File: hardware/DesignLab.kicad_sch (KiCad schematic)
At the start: 79 parts

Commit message: Update BOM
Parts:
- BT1, BT2, BT3, BT4: Stock en EC (none) -> No; manf# (none) -> 534-2477; provedor (none) -> MOUSER
- RV1: LCSC# C99198 -> (none); Stock en EC Yes -> No; manf# (none) -> MCP4017T-103E/LT; provedor LCSC -> MOUSER
- SW1, SW13, SW2: Stock en EC (none) -> No; manf# (none) -> JS102011SAQN; provedor (none) -> MOUSER
- SW10, SW11, SW3, SW4, SW5, SW6, SW7, SW8, SW9: Stock en EC (none) -> No; manf# (none) -> EVQ-PLFA08; provedor (none) -> MOUSER
- SW12: Stock en EC (none) -> No; manf# (none) -> TL3342F450QG; provedor (none) -> MOUSER
- U2: provedor (none) -> MOUSER
- U3, U4, U5: manf# QRE1113GR -> QRE1113; provedor LCSC -> MOUSER
- U6: manf# AT25SF128A-MHB-T -> AT25SF128A-SHB-T
- U8: LCSC# C51118 -> (none); manf# AP2112K-3.3TRG1 -> AP7347DQ-33W5-7; provedor LCSC -> MOUSER

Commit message: Add Micro SD, digital Pot
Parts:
- removed BT1, BT2, BT3: (no value), symbol Device:Battery_Cell
- removed RV1: (no value), symbol Device:R_Potentiometer
- added C?: 100nF, Capacitor_SMD:C_0603_1608Metric, symbol Device:C_Small
- added J?: Micro_SD_Card_Det, symbol Connector:Micro_SD_Card_Det
- added R?: 100K, symbol Device:R_Small
- added SW?: Button, symbol Switch:SW_Push
- added U?: MCP4018-xxxxLT, Package_TO_SOT_SMD:SOT-363_SC-70-6, symbol Potentiometer_Digital:MCP4018-xxxxLT
- BT4: value (none) -> Battery_Cell
- BZ1: value (none) -> Buzzer
- C1, C3: value (none) -> 27pF; footprint (none) -> Capacitor_SMD:C_0603_1608Metric
- C10, C11, C12, C13, C14, C15, C16, C5, C6, C8, C9: value (none) -> 100nF; footprint (none) -> Capacitor_SMD:C_0402_1005Metric_Pad0.74x0.62mm_HandSolder
- C17, C18, C19: value (none) -> 10nF; footprint (none) -> Capacitor_SMD:C_0603_1608Metric
- C2: value (none) -> 0.1uF; footprint (none) -> Capacitor_SMD:C_0402_1005Metric_Pad0.74x0.62mm_HandSolder
- C20: value (none) -> 47uF; footprint (none) -> Capacitor_SMD:C_0603_1608Metric
- C21, C22, C4, C7: value (none) -> 1uF; footprint (none) -> Capacitor_SMD:C_0603_1608Metric
- C23, C24: value (none) -> 220pF; footprint (none) -> Capacitor_SMD:C_0603_1608Metric
- C25, C26, C27: value (none) -> 10uF; footprint (none) -> Capacitor_SMD:C_0402_1005Metric_Pad0.74x0.62mm_HandSolder
- D1: value (none) -> MBR120; footprint (none) -> Diode_SMD:D_SOD-123F
- F1: value (none) -> 0.5A; footprint (none) -> Fuse:Fuse_0805_2012Metric
- JP1: value (none) -> BOOT; footprint (none) -> Jumper:SolderJumper-2_P1.3mm_Open_Pad1.0x1.5mm
- P1: value (none) -> USB_C_Plug_USB2.0; footprint (none) -> Connectors:C393939
- Q1: value (none) -> DMG3415U-7; footprint (none) -> Package_TO_SOT_SMD:SOT-23
- R1: value (none) -> 1K; footprint (none) -> Resistor_SMD:R_0603_1608Metric
- R10, R11, R12: value (none) -> 220; footprint (none) -> Capacitor_SMD:C_0603_1608Metric
- R13: value (none) -> 1.8K; footprint (none) -> Resistor_SMD:R_0603_1608Metric
- R14, R15, R9: value (none) -> 100; footprint (none) -> Resistor_SMD:R_0603_1608Metric
- R16: value (none) -> 10K; footprint (none) -> Resistor_SMD:R_0603_1608Metric
- R17: value (none) -> 100K; footprint (none) -> Resistor_SMD:R_0603_1608Metric
- R18, R19: value (none) -> 5k1; footprint (none) -> Resistor_SMD:R_0603_1608Metric
- R2, R3: value (none) -> 27; footprint (none) -> Resistor_SMD:R_0603_1608Metric
- R4, R6, R7: value (none) -> 100; footprint (none) -> Capacitor_SMD:C_0603_1608Metric
- R5: value (none) -> 4K7; footprint (none) -> Resistor_SMD:R_0603_1608Metric
- R8: value (none) -> 220; footprint (none) -> Resistor_SMD:R_0603_1608Metric
- SW1, SW2: value (none) -> SW_DPDT_x2
- SW10, SW11, SW3, SW4, SW5, SW6, SW7, SW8, SW9: value (none) -> Button
- SW12: value (none) -> RESET
- SW13: value (none) -> ON
- U1: value (none) -> SPH0641LM4H; footprint (none) -> Sensors:MIC_SPH0641LM4H-1
- U2: value (none) -> RP2040; footprint (none) -> badge_pwnCon:RP2040-QFN-56
- U3, U4, U5: value (none) -> QRE1113; footprint (none) -> Package_DIP:SMDIP-4_W7.62mm
- U6: value (none) -> AT25SF128A
- U7: value (none) -> PAM8302AAD; footprint (none) -> Package_SO:MSOP-8_3x3mm_P0.65mm
- U8: value (none) -> AP2112K-3.3; footprint (none) -> Package_TO_SOT_SMD:SOT-23-5
- Y1: value (none) -> 12Mhz; footprint (none) -> Crystal:Crystal_SMD_HC49-SD
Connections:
- net +3V3: now also C?.1, J?.4 (VDD), R?.1, U?.1 (VDD)
- net D4: now also U2.4 (GPIO2); no longer U2.28 (GPIO17)
- net GND: now also BT4.2 (-), C?.2, J?.11 (SHIELD), J?.6 (VSS), J?.9 (DET_B), SW?.1, U?.2 (VSS)
- net GP18: now also U2.17 (GPIO14); no longer U2.29 (GPIO18)
- net REC: now also U2.5 (GPIO3); no longer U2.7 (GPIO5)
- net A: now reaches C20.2, R13.1
- net A: now also U?.6 (A)
- net at C21.1: now also U?.5 (W)
- net CD: now reaches U2.18 (GPIO15)
- net CD: now also J?.10 (DET_A)
- net CIPO: now reaches U2.27 (GPIO16)
- net CIPO: now also J?.7 (DAT0)
- net VOL: now reaches U2.3 (GPIO1)
- net VOL: now also SW?.2
- net COPI: now reaches U2.30 (GPIO19)
- net COPI: now also J?.3 (CMD)
- net SDA: now reaches U2.6 (GPIO4)
- net SDA: now also U?.3 (SCL)
- new net CS: J?.2 (DAT3/CD), R?.2, U2.28 (GPIO17)
- new net CSK: J?.5 (CLK)
- new net SCK: U2.29 (GPIO18)
- new net SCL: U2.7 (GPIO5), U?.4 (SDA)
- no-connect marks 12 -> 9
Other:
- note removed: "Cambiar por AT25SF128A-MHB-T con emapque compatible"
- moved on the sheet: BZ1, C15, C16, C17, C18, C19, C20, C21, C22, C23, C24, C25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

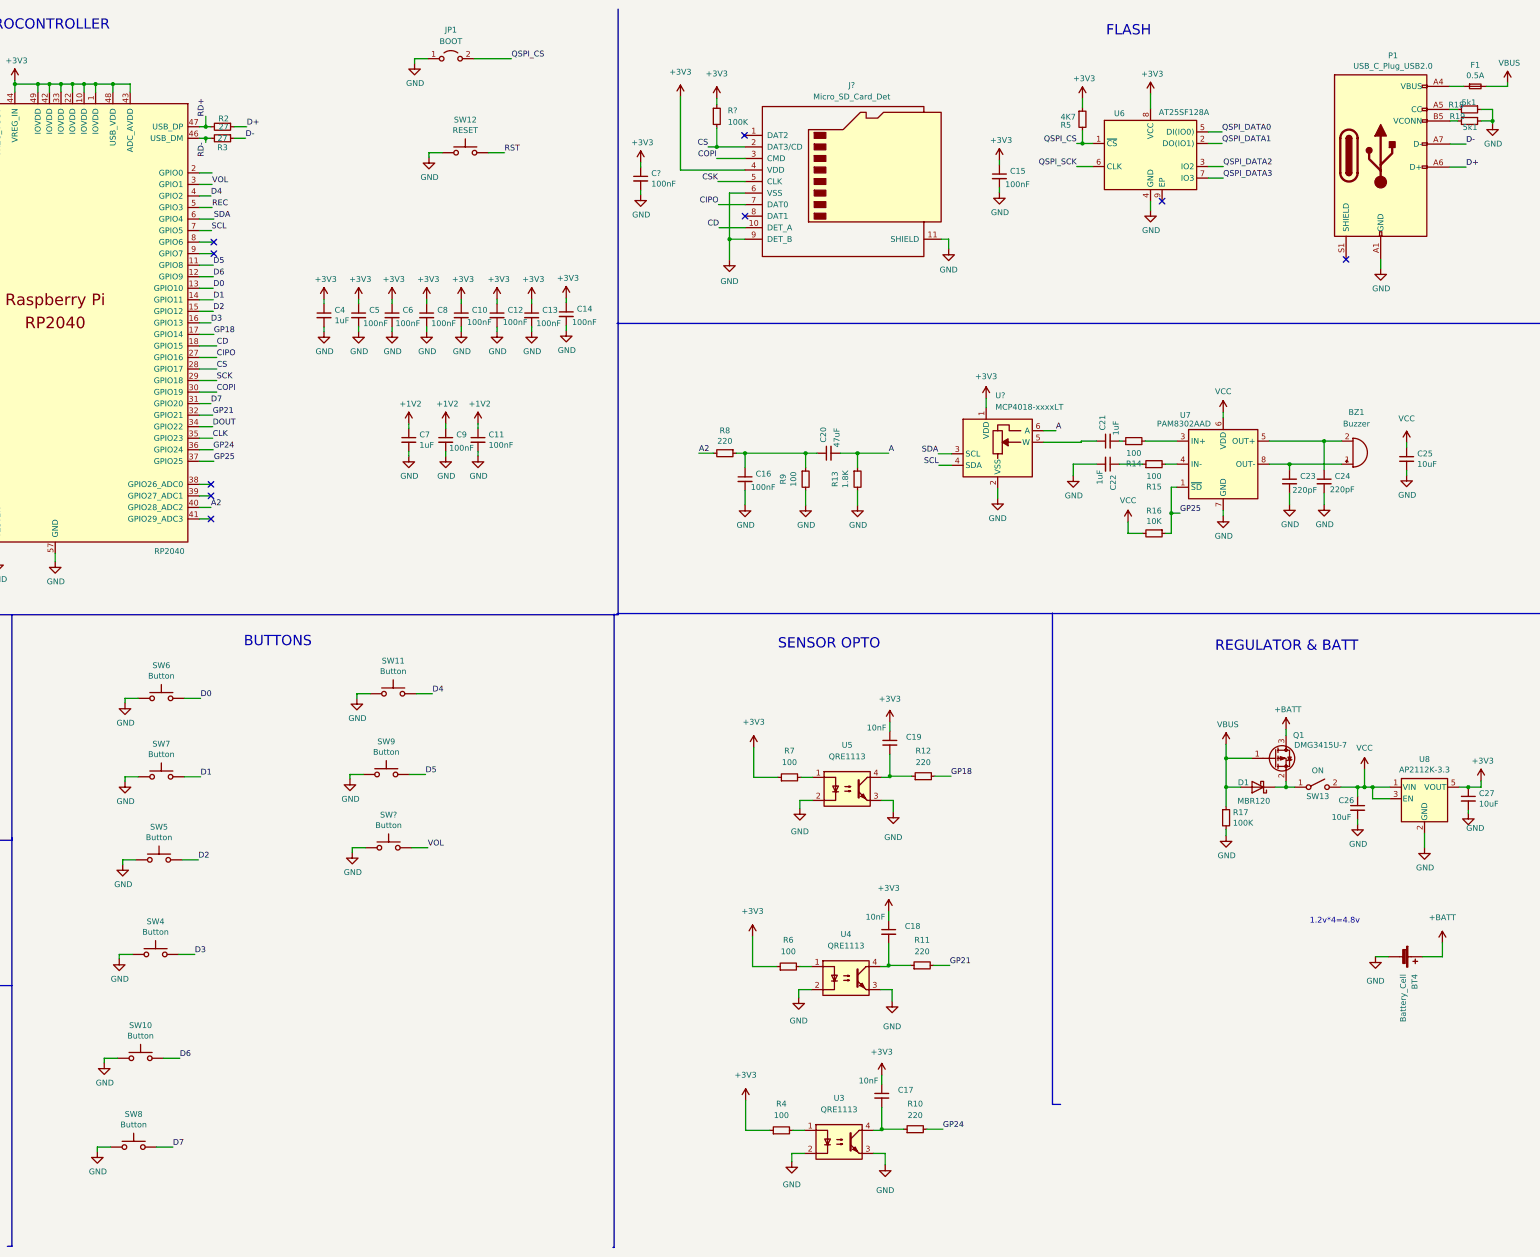
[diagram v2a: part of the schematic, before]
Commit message: add sensor and change button reset
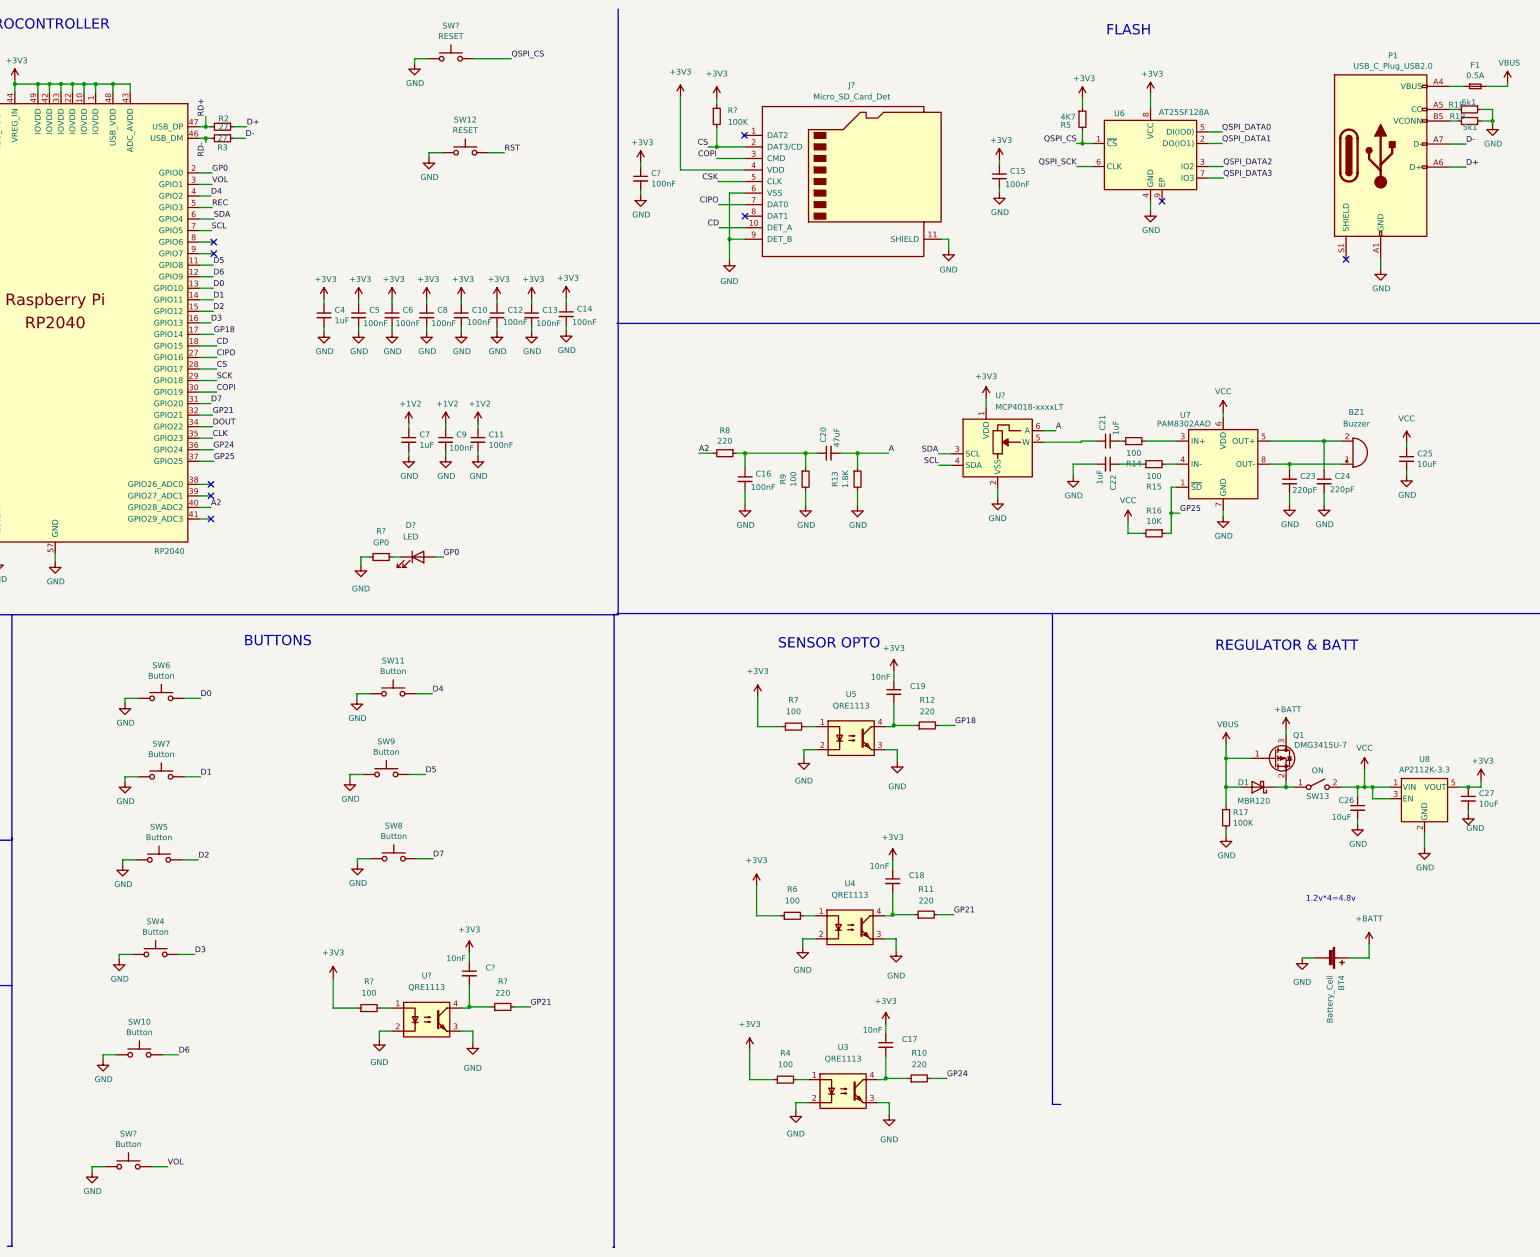
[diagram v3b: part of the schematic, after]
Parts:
- removed JP1: BOOT, Jumper:SolderJumper-2_P1.3mm_Open_Pad1.0x1.5mm, symbol Jumper:Jumper_2_Open
- added C?: 10nF, Capacitor_SMD:C_0603_1608Metric, symbol Device:C_Small
- added D?: LED, symbol Device:LED
- added R?: GP0, symbol Device:R_Small
- added R?: 220, Capacitor_SMD:C_0603_1608Metric, symbol Device:R_Small
- added R?: 100, Capacitor_SMD:C_0603_1608Metric, symbol Device:R_Small
- added SW?: RESET, symbol Switch:SW_Push
- added U?: QRE1113, Package_DIP:SMDIP-4_W7.62mm, symbol Isolator:SFH617A-2X009T
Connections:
- net +3V3: now also C?.1, R?.1
- net GND: now also R?.2, SW?.1, U?.2, U?.3
- net GP21: now also R?.2
- net QSPI_CS: now also SW?.2
- net GP0: now reaches U2.2 (GPIO0)
- net GP0: now also D?.2 (A)
- new net: D?.1 (K), R?.1
- new net: C?.2, R?.1, U?.4
- new net: R?.2, U?.1
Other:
- moved on the sheet: BT4, C17, C18, C19, R10, R11, R12, R4, R6, R7, SW10, SW8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

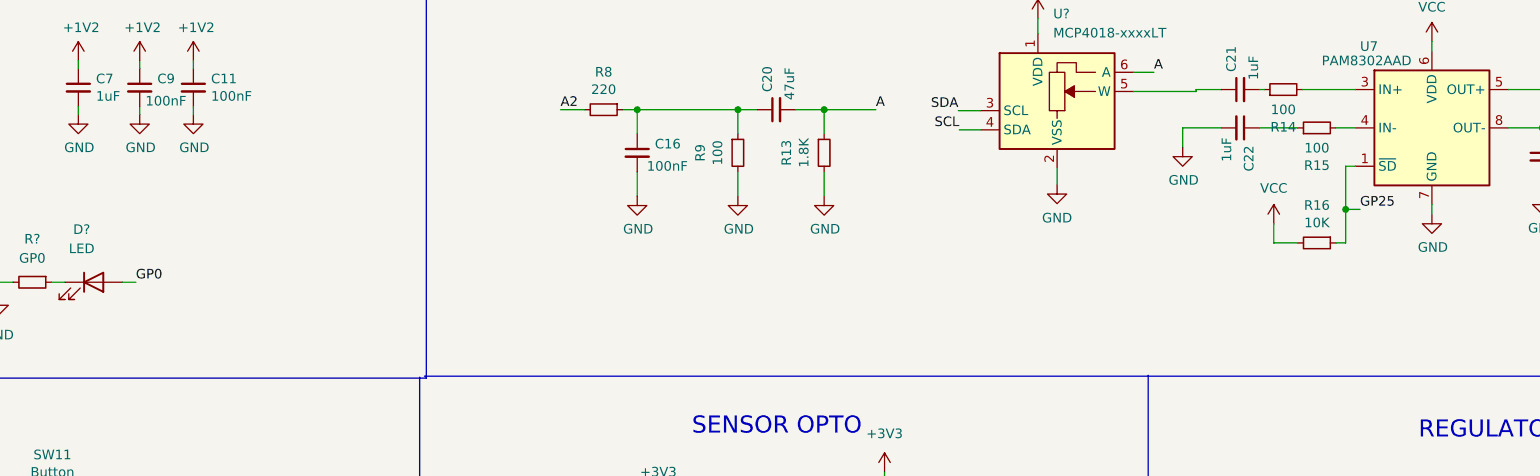
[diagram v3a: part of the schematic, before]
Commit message: change LED_BUILTIN
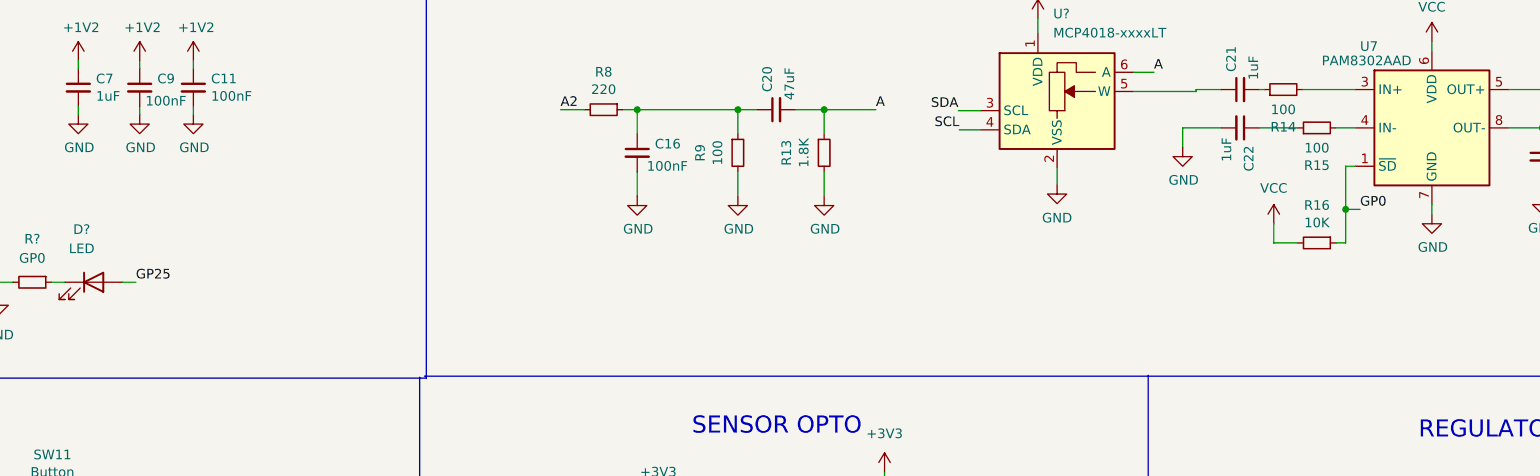
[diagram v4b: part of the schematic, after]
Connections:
- net GP0: now also R16.1, U7.1 (~{SD}); no longer D?.2 (A)
- net GP25: now also D?.2 (A); no longer R16.1, U7.1 (~{SD})
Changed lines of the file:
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@@
     (effects (font (size 1.27 1.27)) (justify left bottom))
   )
-  (label "GP25" (at 327.279 123.063 0)
+  (label "GP0" (at 327.279 123.063 0)
     (effects (font (size 1.27 1.27)) (justify left bottom))
   )
@@
     (effects (font (size 1.27 1.27)) (justify left bottom))
   )
-  (label "GP0" (at 165.1 132.715 0)
+  (label "GP25" (at 165.1 132.715 0)
     (effects (font (size 1.27 1.27)) (justify left bottom))
   )

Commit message: fix buttons
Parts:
- added J?: Conn_01x04_Female, symbol Connector:Conn_01x04_Female
- R?: value GP0 -> 330
- SW?: value RESET -> BOOT
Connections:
- net GP18 is gone; now on net S1: R12.2, U2.17 (GPIO14)
- net +3V3: now also J?.1 (Pin_1)
- net GND: now also J?.4 (Pin_4)
- net SWCLK: now also J?.2 (Pin_2)
- net SWDIO: now also J?.3 (Pin_3)
- net LANG: now reaches U2.38 (GPIO26_ADC0)
- net LANG: now also SW2.2 (B)
- net WORD: now reaches U2.39 (GPIO27_ADC1)
- net WORD: now also SW1.2 (B)
- net S4: now reaches U2.8 (GPIO6)
- net S4: now also R?.2
- removed net GP: SW1.2 (B), SW2.2 (B)
- net GP0 renamed S1
- net S1: no longer U2.2 (GPIO0)
- removed net GP21: R11.2, R?.2, U2.32 (GPIO21)
- net GP24 renamed S2
- net S2: now also R11.2; no longer R10.2
- new net EN_SOUND: U2.2 (GPIO0)
- new net S3: R10.2, U2.32 (GPIO21)
- no-connect marks 9 -> 6
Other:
- note added: "SWD"
- moved on the sheet: BT4, C26, C27, C?, D1, Q1, R17, R?, SW13, U8, U?

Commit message: Assigned footprints
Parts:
- BT4: value Battery_Cell -> (none)
- BZ1: value Buzzer -> (none)
- C1, C3: value 27pF -> (none); footprint Capacitor_SMD:C_0603_1608Metric -> (none)
- C10, C11, C12, C13, C14, C15, C16, C5, C6, C8, C9: value 100nF -> (none); footprint Capacitor_SMD:C_0402_1005Metric_Pad0.74x0.62mm_HandSolder -> (none)
- C17, C18, C19: value 10nF -> (none); footprint Capacitor_SMD:C_0603_1608Metric -> (none)
- C2: value 0.1uF -> (none); footprint Capacitor_SMD:C_0402_1005Metric_Pad0.74x0.62mm_HandSolder -> (none)
- C20: value 47uF -> (none); footprint Capacitor_SMD:C_0603_1608Metric -> (none)
- C21, C22, C4, C7: value 1uF -> (none); footprint Capacitor_SMD:C_0603_1608Metric -> (none)
- C23, C24: value 220pF -> (none); footprint Capacitor_SMD:C_0603_1608Metric -> (none)
- C25, C26, C27: value 10uF -> (none); footprint Capacitor_SMD:C_0402_1005Metric_Pad0.74x0.62mm_HandSolder -> (none)
- C28: renamed from C?; value 10nF -> (none); footprint Capacitor_SMD:C_0603_1608Metric -> (none)
- C29: renamed from C?; value 100nF -> (none); footprint Capacitor_SMD:C_0603_1608Metric -> (none); LCSC# C26413 -> C106209; manf# CL10A105KP8NNNC -> CC0402ZRY5V7BB104
- D1: value MBR120 -> (none); footprint Diode_SMD:D_SOD-123F -> (none)
- D2: renamed from D?; value LED -> (none)
- F1: value 0.5A -> (none); footprint Fuse:Fuse_0805_2012Metric -> (none)
- J1: renamed from J?; value Micro_SD_Card_Det -> (none); Stock en EC (none) -> No
- J2: renamed from J?; value Conn_01x04_Female -> (none)
- P1: value USB_C_Plug_USB2.0 -> (none); footprint Connectors:C393939 -> (none)
- Q1: value DMG3415U-7 -> (none); footprint Package_TO_SOT_SMD:SOT-23 -> (none)
- R1: value 1K -> (none); footprint Resistor_SMD:R_0603_1608Metric -> (none)
- R10, R11, R12: value 220 -> (none); footprint Capacitor_SMD:C_0603_1608Metric -> (none)
- R13: value 1.8K -> (none); footprint Resistor_SMD:R_0603_1608Metric -> (none)
- R14, R15, R9: value 100 -> (none); footprint Resistor_SMD:R_0603_1608Metric -> (none)
- R16: value 10K -> (none); footprint Resistor_SMD:R_0603_1608Metric -> (none)
- R17: value 100K -> (none); footprint Resistor_SMD:R_0603_1608Metric -> (none); manf# RC0603JR-07100KL -> (none)
- R18, R19: value 5k1 -> (none); footprint Resistor_SMD:R_0603_1608Metric -> (none)
- R2, R3: value 27 -> (none); footprint Resistor_SMD:R_0603_1608Metric -> (none)
- R20: renamed from R?; value 330 -> (none)
- R21: renamed from R?; value 100 -> (none); footprint Capacitor_SMD:C_0603_1608Metric -> (none)
- R22: renamed from R?; value 220 -> (none); footprint Capacitor_SMD:C_0603_1608Metric -> (none)
- R23: renamed from R?; value 100K -> (none); LCSC# (none) -> C100048; Stock en EC (none) -> Yes; provedor (none) -> LCSC
- R4, R6, R7: value 100 -> (none); footprint Capacitor_SMD:C_0603_1608Metric -> (none)
- R5: value 4K7 -> (none); footprint Resistor_SMD:R_0603_1608Metric -> (none)
- R8: value 220 -> (none); footprint Resistor_SMD:R_0603_1608Metric -> (none)
- SW1, SW2: value SW_DPDT_x2 -> (none); manf# JS102011SAQN -> (none)
- SW10, SW11, SW3, SW4, SW5, SW6, SW7, SW8, SW9: value Button -> (none)
- SW12: value RESET -> (none)
- SW13: value ON -> (none); manf# JS102011SAQN -> (none)
- SW14: renamed from SW?; value Button -> (none)
- SW15: renamed from SW?; value BOOT -> (none)
- U1: value SPH0641LM4H -> (none); footprint Sensors:MIC_SPH0641LM4H-1 -> (none)
- U10: renamed from U?; value MCP4018-xxxxLT -> (none); footprint Package_TO_SOT_SMD:SOT-363_SC-70-6 -> (none); Stock en EC (none) -> No; manf# (none) -> MCP4017T-103E/LT; provedor (none) -> MOUSER
- U2: value RP2040 -> (none); footprint badge_pwnCon:RP2040-QFN-56 -> (none)
- U3, U4, U5: value QRE1113 -> (none); footprint Package_DIP:SMDIP-4_W7.62mm -> (none); LCSC# C232862 -> (none)
- U6: value AT25SF128A -> (none)
- U7: value PAM8302AAD -> (none); footprint Package_SO:MSOP-8_3x3mm_P0.65mm -> (none)
- U8: value AP2112K-3.3 -> (none); footprint Package_TO_SOT_SMD:SOT-23-5 -> (none)
- U9: renamed from U?; value QRE1113 -> (none); footprint Package_DIP:SMDIP-4_W7.62mm -> (none); LCSC# C232862 -> (none)
- Y1: value 12Mhz -> (none); footprint Crystal:Crystal_SMD_HC49-SD -> (none)
